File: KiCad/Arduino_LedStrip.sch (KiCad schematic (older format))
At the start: 30 parts, among them J1 Conn_L, J10 Screw_Terminal_01x01, J2 Conn_R, J3 LED0, J4 LED1, J5 LED_WS2812B, J6 Barrel_Jack, J7 Screw_Terminal_01x01, J8 Screw_Terminal_01x01, J9 Screw_Terminal_01x01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

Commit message: Update schematic. Change NMOS_GSD to GDS (TO220). Change 5V IR
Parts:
- Q1, Q2, Q3, Q4, Q5, Q6: symbol Q_NMOS_GSD -> Q_NMOS_GDS
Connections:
- net GND: now also Q1.3 (S), Q2.3 (S), Q3.3 (S), Q4.3 (S), Q5.3 (S), Q6.3 (S); no longer Q1.2 (S), Q2.2 (S), Q3.2 (S), Q4.2 (S), Q5.2 (S), Q6.2 (S)
- net LED0_B: now also Q3.2 (D); no longer Q3.3 (D)
- net LED0_G: now also Q2.2 (D); no longer Q2.3 (D)
- net LED0_R: now also Q1.2 (D); no longer Q1.3 (D)
- net LED1_B: now also Q6.2 (D); no longer Q6.3 (D)
- net LED1_G: now also Q5.2 (D); no longer Q5.3 (D)
- net LED1_R: now also Q4.2 (D); no longer Q4.3 (D)
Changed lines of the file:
@@
 ar_LED0_B
 $Comp
-L Q_NMOS_GSD Q3
+L Q_NMOS_GDS Q3
 U 1 1 5A0EAFAA
 P 7050 950
@@
 ar_LED0_B
 $Comp
-L Q_NMOS_GSD Q2
+L Q_NMOS_GDS Q2
 U 1 1 5A0EE48C
 P 5750 950
@@
 ar_LED0_G
 $Comp
-L Q_NMOS_GSD Q1
+L Q_NMOS_GDS Q1
 U 1 1 5A0EE809
 P 4450 950
@@
 ar_A7
 $Comp
-L Q_NMOS_GSD Q6
+L Q_NMOS_GDS Q6
 U 1 1 5A0F1E43
 P 7050 1700
@@
 ar_LED1_B
 $Comp
-L Q_NMOS_GSD Q5
+L Q_NMOS_GDS Q5
 U 1 1 5A0F1E57
 P 5750 1700
@@
 ar_LED1_G
 $Comp
-L Q_NMOS_GSD Q4
+L Q_NMOS_GDS Q4
 U 1 1 5A0F1E6B
 P 4450 1700

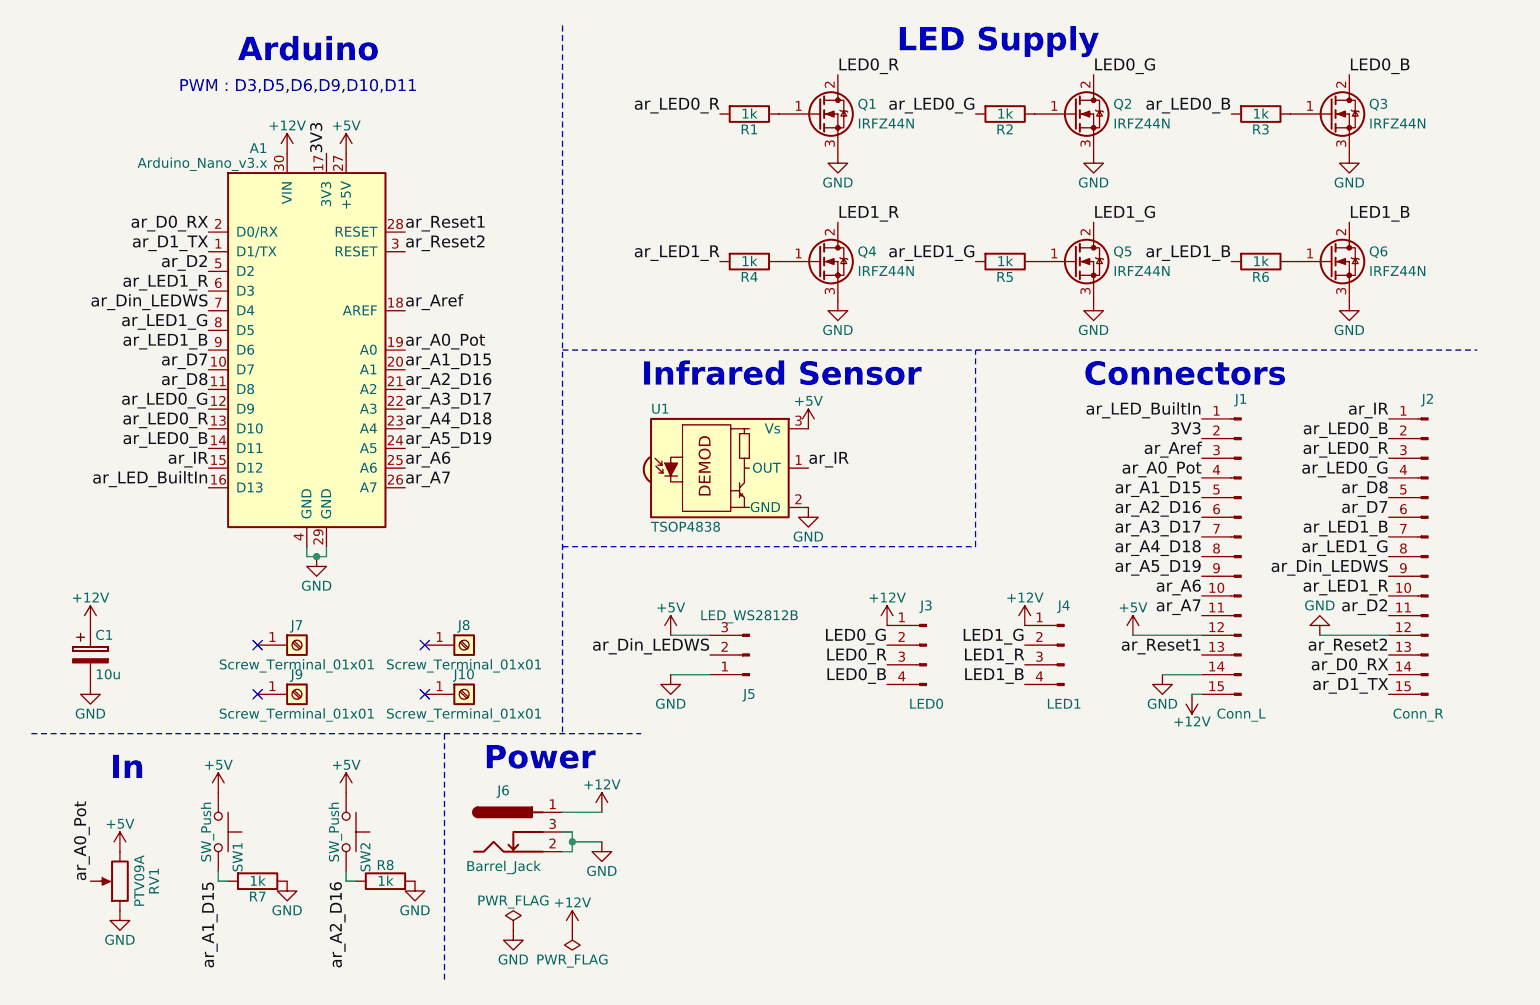
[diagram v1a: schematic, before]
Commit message: Change mode when simple click during animation. Show old value in mode 4 when in settings.
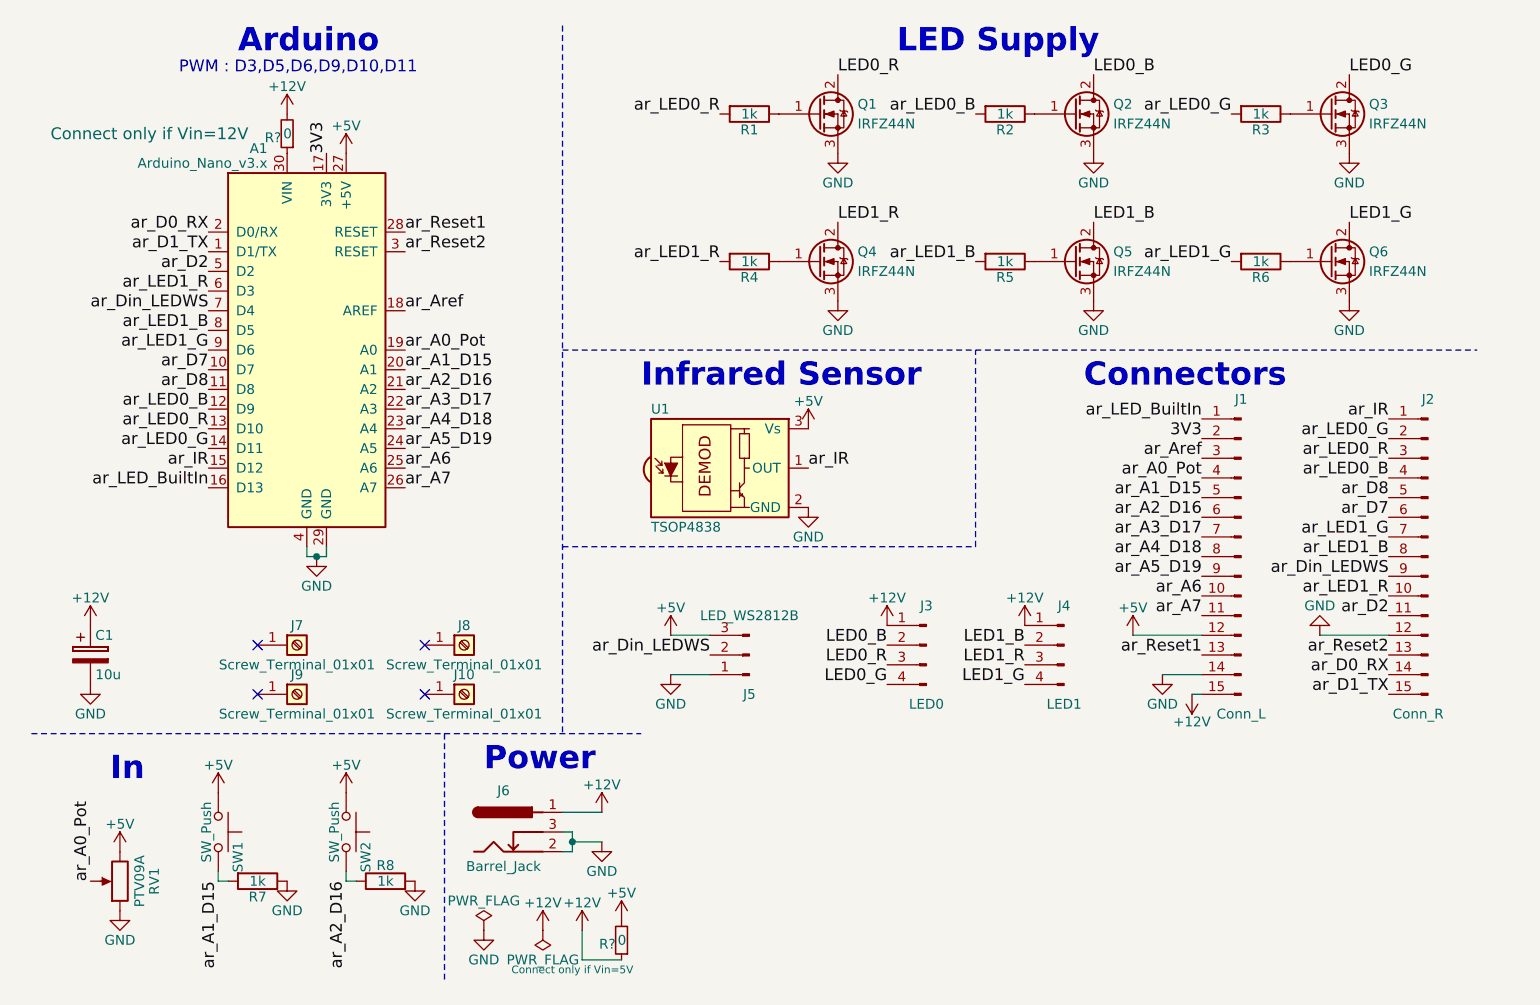
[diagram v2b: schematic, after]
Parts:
- added R? (x2): 0, symbol R_Small
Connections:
- net +12V: now also R?.1, R?.2; no longer A1.30 (VIN)
- net +5V: now also R?.2
- net LED0_B: now also J3.2 (Pin_2), Q2.2 (D); no longer J3.4 (Pin_4), Q3.2 (D)
- net LED0_G: now also J3.4 (Pin_4), Q3.2 (D); no longer J3.2 (Pin_2), Q2.2 (D)
- net LED1_B: now also J4.2 (Pin_2), Q5.2 (D); no longer J4.4 (Pin_4), Q6.2 (D)
- net LED1_G: now also J4.4 (Pin_4), Q6.2 (D); no longer J4.2 (Pin_2), Q5.2 (D)
- net ar_LED0_B: now also A1.12 (D9), J2.4 (Pin_4), R2.2; no longer A1.14 (D11), J2.2 (Pin_2), R3.2
- net ar_LED0_G: now also A1.14 (D11), J2.2 (Pin_2), R3.2; no longer A1.12 (D9), J2.4 (Pin_4), R2.2
- net ar_LED1_B: now also A1.8 (D5), J2.8 (Pin_8), R5.2; no longer A1.9 (D6), J2.7 (Pin_7), R6.2
- net ar_LED1_G: now also A1.9 (D6), J2.7 (Pin_7), R6.2; no longer A1.8 (D5), J2.8 (Pin_8), R5.2
- new net: A1.30 (VIN), R?.1
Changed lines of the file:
@@
 Text Label 1350 2750 2    60   ~ 0
 ar_IR
-Text Notes 1200 850  0    60   ~ 0
+Text Notes 1200 750  0    60   ~ 0
 PWM : D3,D5,D6,D9,D10,D11
 Text Label 1350 1950 2    60   ~ 0
@@
 L +12V #PWR09
 U 1 1 5A0E181E
-P 1750 1150
-F 0 "#PWR09" H 1750 1000 50  0001 C CNN
-F 1 "+12V" H 1750 1290 50  0000 C CNN
-F 2 "" H 1750 1150 50  0001 C CNN
-F 3 "" H 1750 1150 50  0001 C CNN
-	1    1750 1150
+P 1750 950
+F 0 "#PWR09" H 1750 800 50  0001 C CNN
+F 1 "+12V" H 1750 1090 50  0000 C CNN
+F 2 "" H 1750 950 50  0001 C CNN
+F 3 "" H 1750 950 50  0001 C CNN
+	1    1750 950
 	1    0    0    -1
 $EndComp
@@
 ar_LED0_R
 Text Label 1350 2450 2    60   ~ 0
+ar_LED0_B
+Text Label 1350 2650 2    60   ~ 0
 ar_LED0_G
-Text Label 1350 2650 2    60   ~ 0
-ar_LED0_B
 $Comp
 L Q_NMOS_GDS Q3
@@
 $EndComp
 Text Label 7150 750  0    60   ~ 0
-LED0_B
+LED0_G
 Text Label 1350 2850 2    60   ~ 0
 ar_LED_BuiltIn
 Text Label 6550 950  2    60   ~ 0
-ar_LED0_B
+ar_LED0_G
 $Comp
 L Q_NMOS_GDS Q2
@@
 $EndComp
 Text Label 5850 750  0    60   ~ 0
-LED0_G
+LED0_B
 Text Label 5250 950  2    60   ~ 0
-ar_LED0_G
+ar_LED0_B
 $Comp
 L Q_NMOS_GDS Q1
@@
 ar_LED1_R
 Text Label 1350 2050 2    60   ~ 0
+ar_LED1_B
+Text Label 1350 2150 2    60   ~ 0
 ar_LED1_G
-Text Label 1350 2150 2    60   ~ 0
-ar_LED1_B
 Text Label 1350 2250 2    60   ~ 0
 ar_D7
@@
 $EndComp
 Text Label 7150 1500 0    60   ~ 0
-LED1_B
+LED1_G
 Text Label 6550 1700 2    60   ~ 0
-ar_LED1_B
+ar_LED1_G
 $Comp
 L Q_NMOS_GDS Q5
@@
 $EndComp
 Text Label 5850 1500 0    60   ~ 0
-LED1_G
+LED1_B
 Text Label 5250 1700 2    60   ~ 0
-ar_LED1_G
+ar_LED1_B
 $Comp
 L Q_NMOS_GDS Q4
@@
 LED0_R
 Text Label 4800 3650 2    60   ~ 0
+LED0_B
+Text Label 4800 3850 2    60   ~ 0
 LED0_G
-Text Label 4800 3850 2    60   ~ 0
-LED0_B
 $Comp
 L +12V #PWR020
@@
 LED1_R
 Text Label 5500 3650 2    60   ~ 0
+LED1_B
+Text Label 5500 3850 2    60   ~ 0
 LED1_G
-Text Label 5500 3850 2    60   ~ 0
-LED1_B
 $Comp
 L Conn_01x15_Male J2
@@
 ar_LED0_R
 Text Label 7350 2800 2    60   ~ 0
+ar_LED0_B
+Text Label 7350 2600 2    60   ~ 0
 ar_LED0_G
-Text Label 7350 2600 2    60   ~ 0
-ar_LED0_B
 Text Label 7350 3400 2    60   ~ 0
 ar_LED1_R
 Text Label 7350 3200 2    60   ~ 0
+ar_LED1_B
+Text Label 7350 3100 2    60   ~ 0
 ar_LED1_G
-Text Label 7350 3100 2    60   ~ 0
-ar_LED1_B
 Text Label 7350 3000 2    60   ~ 0
 ar_D7
@@
 Text Notes 850  4350 0    118  ~ 24
 In
-Text Notes 1500 700  0    118  ~ 24
+Text Notes 1500 650  0    118  ~ 24
 Arduino
 Text Notes 4850 650  0    118  ~ 24
@@
 L PWR_FLAG #FLG030
 U 1 1 5A117857
-P 2900 5100
-F 0 "#FLG030" H 2900 5175 50  0001 C CNN
-F 1 "PWR_FLAG" H 2900 5250 50  0000 C CNN
-F 2 "" H 2900 5100 50  0001 C CNN
-F 3 "" H 2900 5100 50  0001 C CNN
-	1    2900 5100
+P 2750 5100
+F 0 "#FLG030" H 2750 5175 50  0001 C CNN
+F 1 "PWR_FLAG" H 2750 5250 50  0000 C CNN
+F 2 "" H 2750 5100 50  0001 C CNN
+F 3 "" H 2750 5100 50  0001 C CNN
+	1    2750 5100
 	1    0    0    -1
 $EndComp
@@
 L GND #PWR031
 U 1 1 5A1178B7
-P 2900 5100
-F 0 "#PWR031" H 2900 4850 50  0001 C CNN
-F 1 "GND" H 2900 4950 50  0000 C CNN
-F 2 "" H 2900 5100 50  0001 C CNN
-F 3 "" H 2900 5100 50  0001 C CNN
-	1    2900 5100
+P 2750 5100
+F 0 "#PWR031" H 2750 4850 50  0001 C CNN
+F 1 "GND" H 2750 4950 50  0000 C CNN
+F 2 "" H 2750 5100 50  0001 C CNN
+F 3 "" H 2750 5100 50  0001 C CNN
+	1    2750 5100
 	1    0    0    -1
 $EndComp
@@
 L +12V #PWR032
 U 1 1 5A118832
-P 3200 5100
-F 0 "#PWR032" H 3200 4950 50  0001 C CNN
-F 1 "+12V" H 3200 5240 50  0000 C CNN
-F 2 "" H 3200 5100 50  0001 C CNN
-F 3 "" H 3200 5100 50  0001 C CNN
-	1    3200 5100
+P 3050 5100
+F 0 "#PWR032" H 3050 4950 50  0001 C CNN
+F 1 "+12V" H 3050 5240 50  0000 C CNN
+F 2 "" H 3050 5100 50  0001 C CNN
+F 3 "" H 3050 5100 50  0001 C CNN
+	1    3050 5100
 	1    0    0    -1
 $EndComp
@@
 L PWR_FLAG #FLG033
 U 1 1 5A11888B
-P 3200 5100
-F 0 "#FLG033" H 3200 5175 50  0001 C CNN
-F 1 "PWR_FLAG" H 3200 5250 50  0000 C CNN
-F 2 "" H 3200 5100 50  0001 C CNN
-F 3 "" H 3200 5100 50  0001 C CNN
-	1    3200 5100
+P 3050 5100
+F 0 "#FLG033" H 3050 5175 50  0001 C CNN
+F 1 "PWR_FLAG" H 3050 5250 50  0000 C CNN
+F 2 "" H 3050 5100 50  0001 C CNN
+F 3 "" H 3050 5100 50  0001 C CNN
+	1    3050 5100
 	-1   0    0    1
 $EndComp
@@
 NoConn ~ 2450 3900
 NoConn ~ 1600 3900
+$Comp
+L R_Small R?
+U 1 1 5A5A585B
+P 1750 1050
+F 0 "R?" H 1780 1070 50  0000 L CNN
+F 1 "0" H 1726 1050 50  0000 L CNN
+F 2 "" H 1750 1050 50  0001 C CNN
+F 3 "" H 1750 1050 50  0001 C CNN
+F 4 "Connect only if Vin=12V" H 2450 1050 60  0000 C CNN "Info"
+	1    1750 1050
+	-1   0    0    1
+$EndComp
+$Comp
+L R_Small R?
+U 1 1 5A5A6B65
+P 3450 5150
+F 0 "R?" H 3480 5170 50  0000 L CNN
+F 1 "0" H 3426 5150 50  0000 L CNN
+F 2 "" H 3450 5150 50  0001 C CNN
+F 3 "" H 3450 5150 50  0001 C CNN
+F 4 "Connect only if Vin=5V" H 3700 5300 39  0000 C CNN "Info"
+	1    3450 5150
+	-1   0    0    1
+$EndComp
+$Comp
+L +12V #PWR?
+U 1 1 5A5A6FAA
+P 3250 5100
+F 0 "#PWR?" H 3250 4950 50  0001 C CNN
+F 1 "+12V" H 3250 5240 50  0000 C CNN
+F 2 "" H 3250 5100 50  0001 C CNN
+F 3 "" H 3250 5100 50  0001 C CNN
+	1    3250 5100
+	1    0    0    -1
+$EndComp
+Wire Wire Line
+	3250 5100 3250 5250
+Wire Wire Line
+	3250 5250 3450 5250
+$Comp
+L +5V #PWR?
+U 1 1 5A5A73E7
+P 3450 5050
+F 0 "#PWR?" H 3450 4900 50  0001 C CNN
+F 1 "+5V" H 3450 5190 50  0000 C CNN
+F 2 "" H 3450 5050 50  0001 C CNN
+F 3 "" H 3450 5050 50  0001 C CNN
+	1    3450 5050
+	1    0    0    -1
+$EndComp
 $EndSCHEMATC

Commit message: Add possibility to use a 5V or 12V power. Create new gerbers
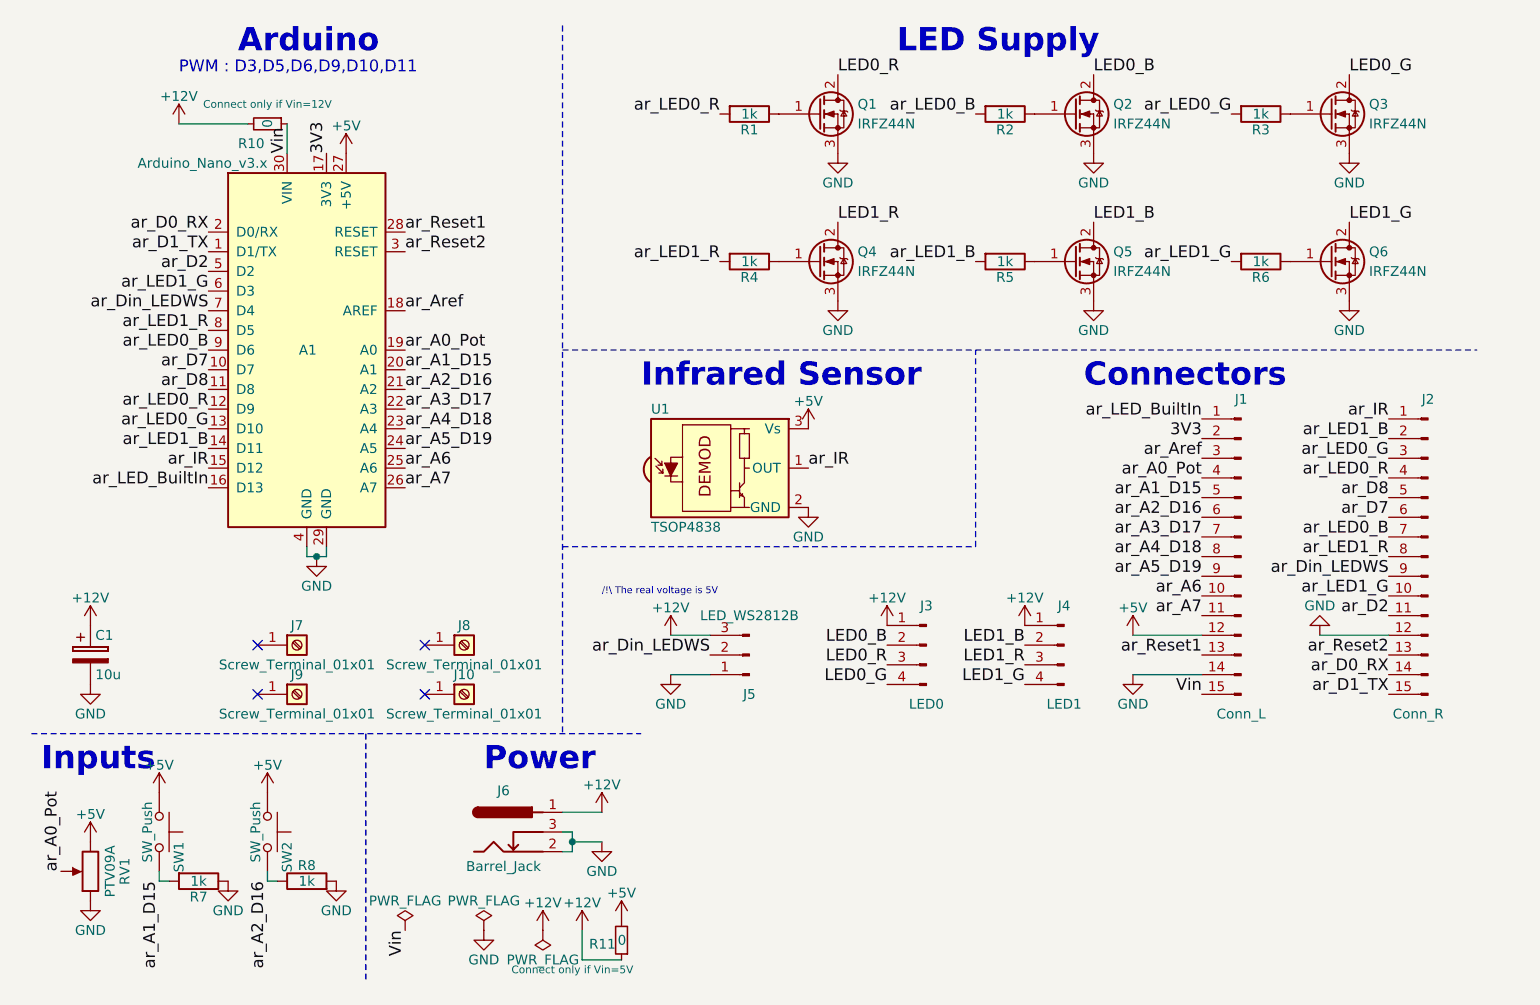
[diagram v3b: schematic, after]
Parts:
- R10, R11: renamed from R?; footprint (none) -> Battery_pads:R_Shunt
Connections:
- net +12V: now also J5.3 (Pin_3); no longer J1.15 (Pin_15)
- net +5V: no longer J5.3 (Pin_3)
- net ar_LED0_B: now also A1.9 (D6), J2.7 (Pin_7); no longer A1.12 (D9), J2.4 (Pin_4)
- net ar_LED0_G: now also A1.13 (D10), J2.3 (Pin_3); no longer A1.14 (D11), J2.2 (Pin_2)
- net ar_LED0_R: now also A1.12 (D9), J2.4 (Pin_4); no longer A1.13 (D10), J2.3 (Pin_3)
- net ar_LED1_B: now also A1.14 (D11), J2.2 (Pin_2); no longer A1.8 (D5), J2.8 (Pin_8)
- net ar_LED1_G: now also A1.6 (D3), J2.10 (Pin_10); no longer A1.9 (D6), J2.7 (Pin_7)
- net ar_LED1_R: now also A1.8 (D5), J2.8 (Pin_8); no longer A1.6 (D3), J2.10 (Pin_10)
- net Vin: now reaches A1.30 (VIN), R10.1
- net Vin: now also J1.15 (Pin_15)
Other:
- note added: "/!\ The real voltage is 5V"
- note added: "Inputs"
- note removed: "In"
- moved on the sheet: R10, R7, R8, RV1, SW1, SW2

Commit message: Update folder paths. Add Wemos.
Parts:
- removed J1: Conn_L, Pin_Headers:Pin_Header_Straight_1x15_Pitch2.54mm, symbol Conn_01x15_Male
- removed J10: Screw_Terminal_01x01, Mounting_Holes:MountingHole_3.2mm_M3, symbol Screw_Terminal_01x01
- removed J2: Conn_R, Pin_Headers:Pin_Header_Straight_1x15_Pitch2.54mm, symbol Conn_01x15_Male
- added R12, R9: 1kor0, Resistors_SMD:R_0603_HandSoldering, symbol R_Small
- added U2: L7805, TO_SOT_Packages_THT:TO-220-3_Vertical, symbol L7805
- added U3: WeMos_mini, GoInK13:D1_mini_board, symbol WeMos_mini
- R10: Info Connect only if Vin=12V -> Shunt if Vin=12V
- R11: Info Connect only if Vin=5V -> Shunt if Vin=5V
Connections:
- net Vin is gone; now on net +12V: A1.30 (VIN), R10.1
- net ar_Aref is gone; now on net +3V3: A1.18 (AREF)
- net +12V: now also U2.1 (IN); no longer C1.1, J3.1 (Pin_1), J4.1 (Pin_1), J5.3 (Pin_3), J6.1, R10.2, R11.1
- net +5V: now also U2.3 (OUT), U3.1 (5V); no longer RV1.3
- net GND: now also U2.2 (GND), U3.2 (GND)
- net ar_A0_Pot: now also U3.15 (D8)
- net ar_A1_D15: now also R9.1, U3.14 (D7); no longer SW1.2
- net ar_A2_D16: now also R12.1, U3.13 (D6); no longer SW2.2
- net ar_A3_D17: now also U3.12 (D5)
- net ar_Din_LEDWS: now also U3.7 (Rx)
- net ar_IR: now also U3.3 (D4)
- net ar_LED0_B: now also U3.5 (D2)
- net ar_LED0_G: now also U3.10 (A0)
- net ar_LED0_R: now also U3.11 (D0)
- net ar_LED1_B: now also U3.4 (D3)
- net ar_LED1_G: now also U3.8 (Tx)
- net ar_LED1_R: now also U3.6 (D1)
- net 3V3 renamed +3V3
- net +3V3: now also RV1.3, U3.16 (3.3V)
- new net: R12.2, SW2.2
- new net: R9.2, SW1.2
- new net VCC: C1.1, J3.1 (Pin_1), J4.1 (Pin_1), J5.3 (Pin_3), J6.1, R10.2, R11.1
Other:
- note added: "+LDO 12V→5V"
- note added: "/!\ Connect 500Ω to 1kΩ if wemos, else 0"
- note added: "Shunts"
- note added: "Wemos"
- moved on the sheet: J3, J4, J5, J6, R10, R11, R7, RV1, SW1, SW2, U1
